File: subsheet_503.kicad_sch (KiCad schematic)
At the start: 39 parts, among them Q500 LM78L82_TO92, U504 LF347N_mu, U505 MF4CN-100_PHY, U506 MF4CN-100_PHY, U507 LF347N_mu

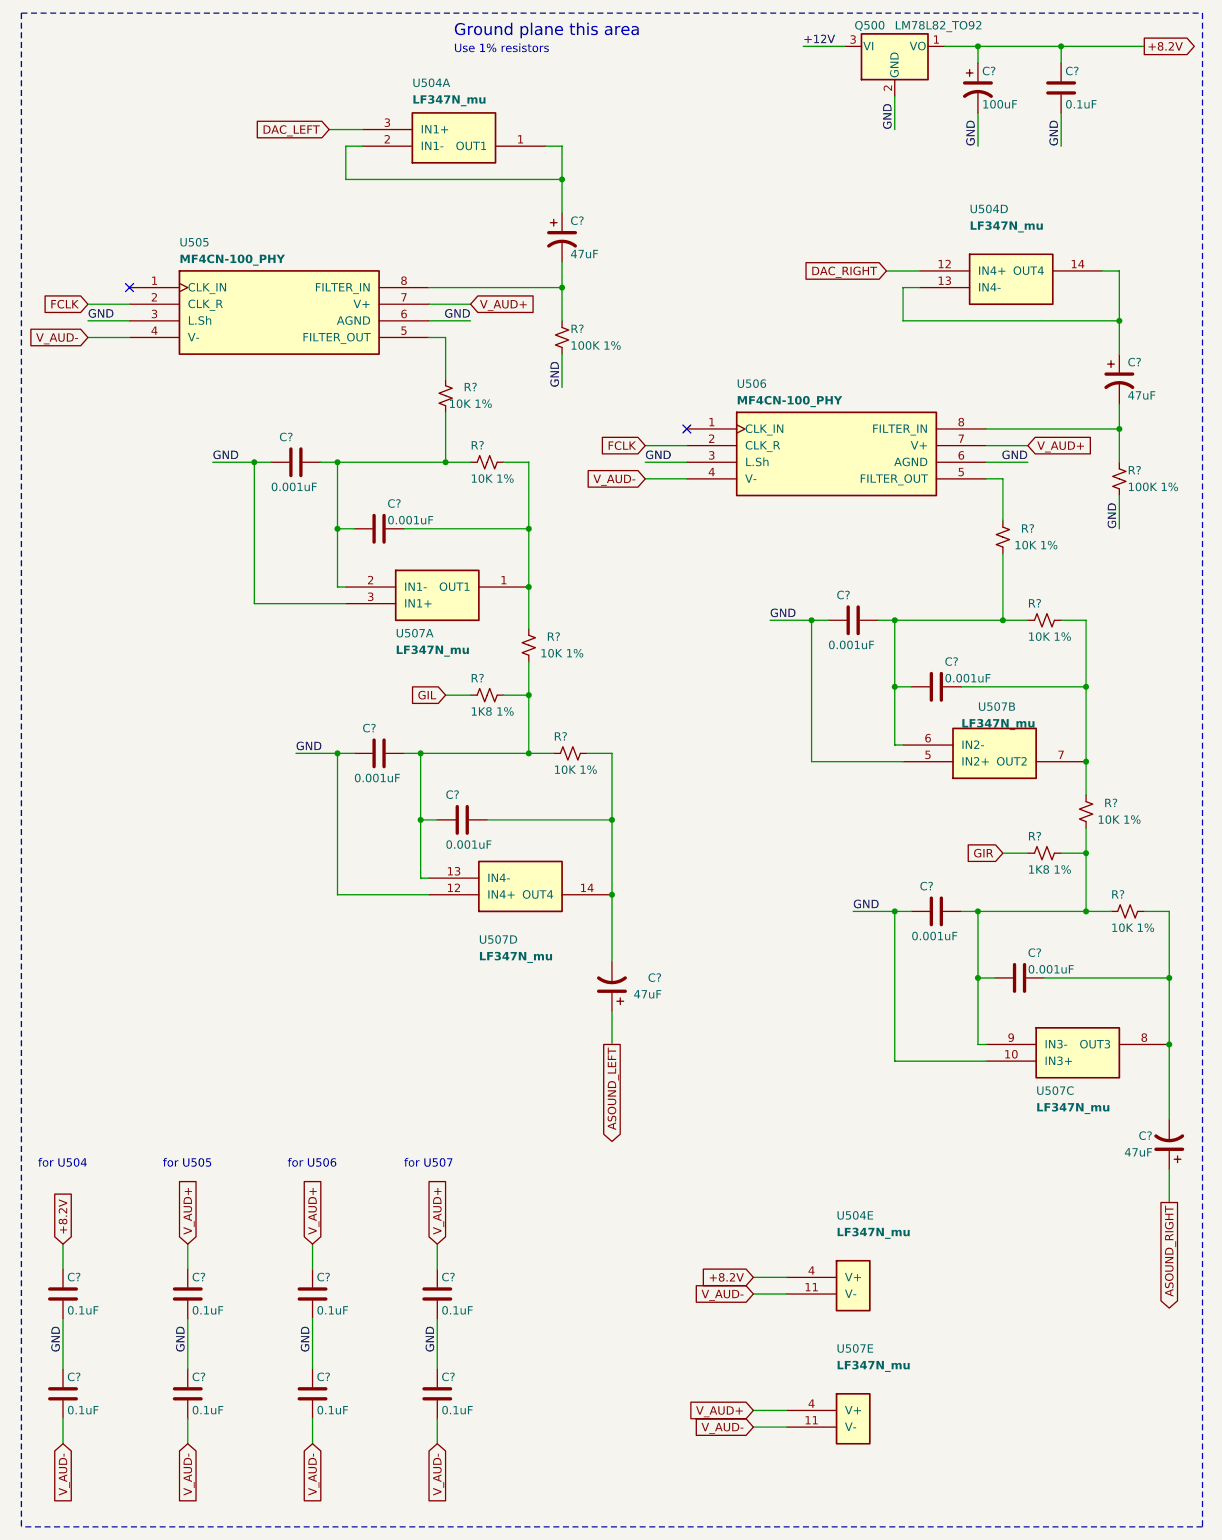
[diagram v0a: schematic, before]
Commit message: Resolves #3 : [schematic] annotate video port with signal name
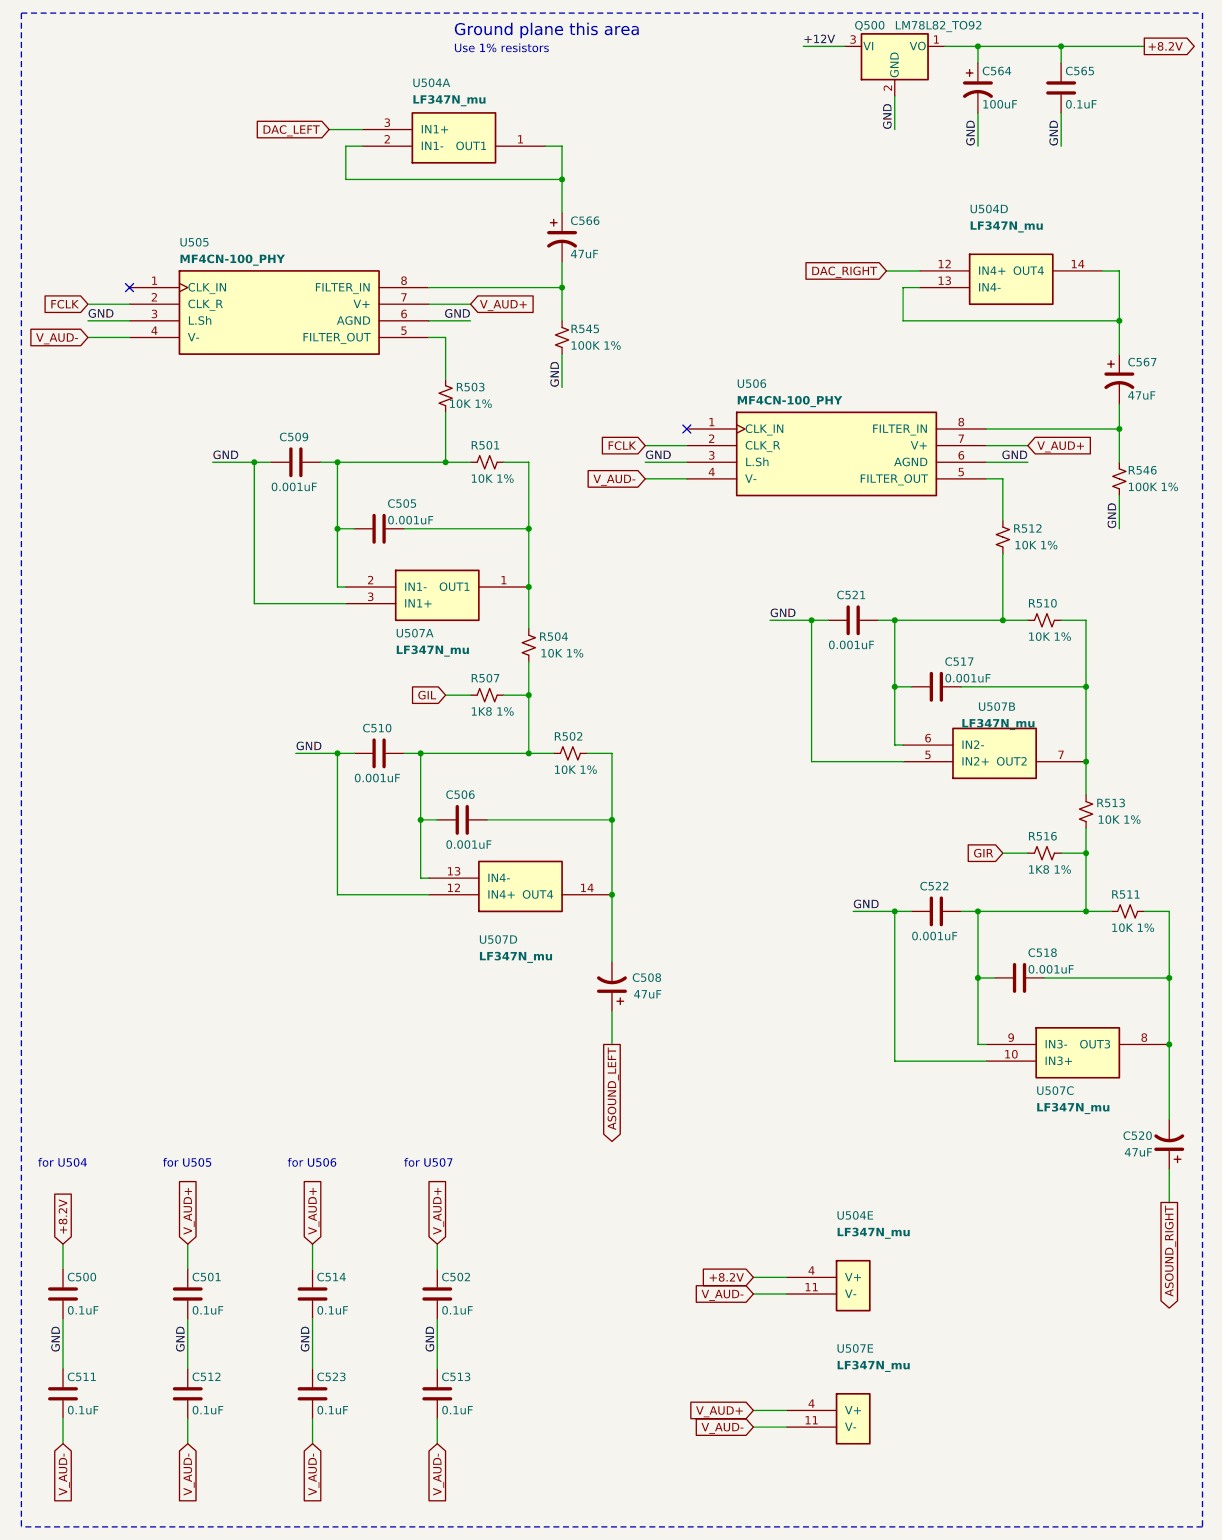
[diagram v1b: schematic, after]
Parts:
- gave numbers to parts that had none: 34
